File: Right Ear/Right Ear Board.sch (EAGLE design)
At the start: 6 parts, among them J1 502585-0470

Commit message: Update right ear boards
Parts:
- removed C2: (no value), rcl:C-USC0402
- added C4: 10uF, rcl:C-USC0603K
- added SV2, SV3: (no value), con-lstb:MA03-1
- C1: value (none) -> 10uF; device rcl:C-USC0402 -> rcl:C-USC0603K; PARTNO (none) -> GRM188R61A106KE69D
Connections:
- removed net N$1: LED1.DO, LED7.DI
- new net DATA: LED1.DO, LED7.DI, SV2.2, SV3.2
- net +5V: now also C4.1, SV2.1, SV3.3; no longer C2.1
- net GND: now also C4.2, SV2.3, SV3.1; no longer C2.2
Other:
- moved on the sheet: C1
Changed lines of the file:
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@@
 <?xml version="1.0" encoding="utf-8"?>
 <!DOCTYPE eagle SYSTEM "eagle.dtd">
-<eagle version="8.6.0">
+<eagle version="8.5.0">
 <drawing>
 <settings>
@@
 <part name="LED7" library="adafruit" deviceset="WS2812B" device="5050"/>
 <part name="LED1" library="adafruit" deviceset="WS2812B" device="5050"/>
-<part name="C1" library="rcl" library_urn="urn:adsk.eagle:library:334" deviceset="C-US" device="C0402" package3d_urn="urn:adsk.eagle:package:23626/1"/>
 <part name="GND20" library="supply1" deviceset="GND" device=""/>
-<part name="C2" library="rcl" library_urn="urn:adsk.eagle:library:334" deviceset="C-US" device="C0402" package3d_urn="urn:adsk.eagle:package:23626/1"/>
 <part name="GND1" library="supply1" deviceset="GND" device=""/>
 <part name="J1" library="FormE" deviceset="MOLEX_CLICKMATE-4-R/A" device="" value="502585-0470"/>
@@
 <part name="P+2" library="supply1" library_urn="urn:adsk.eagle:library:371" deviceset="+5V" device=""/>
 <part name="P+3" library="supply1" library_urn="urn:adsk.eagle:library:371" deviceset="+5V" device=""/>
+<part name="SV2" library="con-lstb" library_urn="urn:adsk.eagle:library:162" deviceset="MA03-1" device="" package3d_urn="urn:adsk.eagle:package:8339/1"/>
+<part name="SV3" library="con-lstb" library_urn="urn:adsk.eagle:library:162" deviceset="MA03-1" device="" package3d_urn="urn:adsk.eagle:package:8339/1"/>
+<part name="C4" library="rcl" deviceset="C-US" device="C0603K" value="10uF">
+<attribute name="PARTNO" value="GRM188R61A106KE69D"/>
+</part>
+<part name="C1" library="rcl" deviceset="C-US" device="C0603K" value="10uF">
+<attribute name="PARTNO" value="GRM188R61A106KE69D"/>
+</part>
+<part name="P+4" library="supply1" library_urn="urn:adsk.eagle:library:371" deviceset="+5V" device=""/>
 </parts>
 <sheets>
@@
 <instances>
 <instance part="SV1" gate="G$1" x="78.74" y="46.99" rot="MR180"/>
-<instance part="LED7" gate="G$1" x="58.42" y="82.55" rot="MR0"/>
+<instance part="LED7" gate="G$1" x="35.56" y="87.63" rot="MR0"/>
 <instance part="LED1" gate="G$1" x="106.68" y="82.55" rot="MR0"/>
-<instance part="C1" gate="G$1" x="81.28" y="97.79"/>
-<instance part="GND20" gate="1" x="81.28" y="90.17"/>
-<instance part="C2" gate="G$1" x="128.27" y="95.25"/>
-<instance part="GND1" gate="1" x="128.27" y="87.63"/>
+<instance part="GND20" gate="1" x="63.5" y="92.71"/>
+<instance part="GND1" gate="1" x="128.27" y="85.09"/>
 <instance part="J1" gate="G$1" x="165.1" y="49.53"/>
-<instance part="GND2" gate="1" x="58.42" y="61.976"/>
+<instance part="GND2" gate="1" x="35.56" y="67.056"/>
 <instance part="GND3" gate="1" x="106.68" y="61.214"/>
 <instance part="GND4" gate="1" x="91.186" y="34.29"/>
 <instance part="GND5" gate="1" x="151.13" y="41.91"/>
 <instance part="P+1" gate="1" x="152.4" y="60.96"/>
-<instance part="P+2" gate="1" x="53.34" y="106.68"/>
+<instance part="P+2" gate="1" x="30.48" y="111.76"/>
 <instance part="P+3" gate="1" x="86.36" y="58.42"/>
+<instance part="SV2" gate="G$1" x="73.66" y="80.01" rot="MR180"/>
+<instance part="SV3" gate="G$1" x="71.12" y="80.01" rot="MR0"/>
+<instance part="C4" gate="G$1" x="63.5" y="101.6">
+<attribute name="PARTNO" x="63.5" y="101.6" size="1.778" layer="96" display="off"/>
+</instance>
+<instance part="C1" gate="G$1" x="128.27" y="94.488">
+<attribute name="PARTNO" x="128.27" y="94.488" size="1.778" layer="96" display="off"/>
+</instance>
+<instance part="P+4" gate="1" x="127" y="106.68"/>
 </instances>
 <busses>
@@
 </segment>
 <segment>
-<pinref part="C1" gate="G$1" pin="1"/>
-<pinref part="LED7" gate="G$1" pin="VDD"/>
-<wire x1="53.34" y1="97.79" x2="53.34" y2="100.33" width="0.1524" layer="91"/>
-<wire x1="53.34" y1="100.33" x2="53.34" y2="104.14" width="0.1524" layer="91"/>
-<wire x1="81.28" y1="100.33" x2="53.34" y2="100.33" width="0.1524" layer="91"/>
-<junction x="53.34" y="100.33"/>
-<pinref part="LED1" gate="G$1" pin="VDD"/>
-<wire x1="101.6" y1="97.79" x2="101.6" y2="100.33" width="0.1524" layer="91"/>
-<wire x1="81.28" y1="100.33" x2="101.6" y2="100.33" width="0.1524" layer="91"/>
-<junction x="81.28" y="100.33"/>
-<junction x="101.6" y="100.33"/>
-<pinref part="C2" gate="G$1" pin="1"/>
-<wire x1="101.6" y1="100.33" x2="128.27" y2="100.33" width="0.1524" layer="91"/>
-<wire x1="128.27" y1="100.33" x2="128.27" y2="97.79" width="0.1524" layer="91"/>
-<pinref part="P+2" gate="1" pin="+5V"/>
-</segment>
-<segment>
 <pinref part="J1" gate="G$1" pin="1"/>
 <wire x1="162.56" y1="54.61" x2="152.4" y2="54.61" width="0.1524" layer="91"/>
@@
 <pinref part="P+1" gate="1" pin="+5V"/>
 </segment>
+<segment>
+<wire x1="128.27" y1="100.33" x2="128.27" y2="97.028" width="0.1524" layer="91"/>
+<wire x1="101.6" y1="100.33" x2="127" y2="100.33" width="0.1524" layer="91"/>
+<pinref part="LED1" gate="G$1" pin="VDD"/>
+<wire x1="127" y1="100.33" x2="128.27" y2="100.33" width="0.1524" layer="91"/>
+<wire x1="101.6" y1="97.79" x2="101.6" y2="99.06" width="0.1524" layer="91"/>
+<pinref part="SV2" gate="G$1" pin="1"/>
+<wire x1="101.6" y1="99.06" x2="101.6" y2="100.33" width="0.1524" layer="91"/>
+<wire x1="81.28" y1="82.55" x2="81.28" y2="99.06" width="0.1524" layer="91"/>
+<wire x1="81.28" y1="99.06" x2="101.6" y2="99.06" width="0.1524" layer="91"/>
+<junction x="101.6" y="99.06"/>
+<pinref part="C1" gate="G$1" pin="1"/>
+<pinref part="P+4" gate="1" pin="+5V"/>
+<wire x1="127" y1="104.14" x2="127" y2="100.33" width="0.1524" layer="91"/>
+<junction x="127" y="100.33"/>
+</segment>
+<segment>
+<pinref part="LED7" gate="G$1" pin="VDD"/>
+<pinref part="P+2" gate="1" pin="+5V"/>
+<wire x1="30.48" y1="102.87" x2="30.48" y2="106.68" width="0.1524" layer="91"/>
+<pinref part="C4" gate="G$1" pin="1"/>
+<wire x1="30.48" y1="106.68" x2="30.48" y2="109.22" width="0.1524" layer="91"/>
+<wire x1="63.5" y1="104.14" x2="63.5" y2="106.68" width="0.1524" layer="91"/>
+<wire x1="63.5" y1="106.68" x2="53.34" y2="106.68" width="0.1524" layer="91"/>
+<junction x="30.48" y="106.68"/>
+<pinref part="SV3" gate="G$1" pin="3"/>
+<wire x1="53.34" y1="106.68" x2="30.48" y2="106.68" width="0.1524" layer="91"/>
+<wire x1="63.5" y1="82.55" x2="53.34" y2="82.55" width="0.1524" layer="91"/>
+<wire x1="53.34" y1="82.55" x2="53.34" y2="106.68" width="0.1524" layer="91"/>
+<junction x="53.34" y="106.68"/>
+</segment>
 </net>
 <net name="GND" class="0">
-<segment>
-<pinref part="C1" gate="G$1" pin="2"/>
-<pinref part="GND20" gate="1" pin="GND"/>
-</segment>
-<segment>
-<pinref part="C2" gate="G$1" pin="2"/>
-<pinref part="GND1" gate="1" pin="GND"/>
-</segment>
 <segment>
 <pinref part="J1" gate="G$1" pin="4"/>
@@
 <pinref part="LED7" gate="G$1" pin="GND"/>
 <pinref part="GND2" gate="1" pin="GND"/>
-<wire x1="58.42" y1="72.39" x2="58.42" y2="64.516" width="0.1524" layer="91"/>
+<wire x1="35.56" y1="77.47" x2="35.56" y2="69.596" width="0.1524" layer="91"/>
+<pinref part="SV3" gate="G$1" pin="1"/>
+<wire x1="63.5" y1="77.47" x2="35.56" y2="77.47" width="0.1524" layer="91"/>
+<junction x="35.56" y="77.47"/>
 </segment>
 <segment>
 <pinref part="LED1" gate="G$1" pin="GND"/>
 <pinref part="GND3" gate="1" pin="GND"/>
-<wire x1="106.68" y1="72.39" x2="106.68" y2="63.754" width="0.1524" layer="91"/>
+<wire x1="106.68" y1="72.39" x2="106.68" y2="71.12" width="0.1524" layer="91"/>
+<pinref part="SV2" gate="G$1" pin="3"/>
+<wire x1="106.68" y1="71.12" x2="106.68" y2="63.754" width="0.1524" layer="91"/>
+<wire x1="81.28" y1="77.47" x2="81.28" y2="71.12" width="0.1524" layer="91"/>
+<wire x1="81.28" y1="71.12" x2="106.68" y2="71.12" width="0.1524" layer="91"/>
+<junction x="106.68" y="71.12"/>
 </segment>
 <segment>
@@
 <wire x1="86.36" y1="44.45" x2="91.186" y2="44.45" width="0.1524" layer="91"/>
 <wire x1="91.186" y1="44.45" x2="91.186" y2="36.83" width="0.1524" layer="91"/>
+</segment>
+<segment>
+<pinref part="GND20" gate="1" pin="GND"/>
+<pinref part="C4" gate="G$1" pin="2"/>
+<wire x1="63.5" y1="95.25" x2="63.5" y2="96.52" width="0.1524" layer="91"/>
+</segment>
+<segment>
+<pinref part="C1" gate="G$1" pin="2"/>
+<pinref part="GND1" gate="1" pin="GND"/>
+<wire x1="128.27" y1="89.408" x2="128.27" y2="87.63" width="0.1524" layer="91"/>
 </segment>
 </net>
@@
 </segment>
 </net>
-<net name="N$1" class="0">
-<segment>
+<net name="DATA" class="0">
+<segment>
+<pinref part="LED1" gate="G$1" pin="DO"/>
+<pinref part="SV2" gate="G$1" pin="2"/>
+<wire x1="93.98" y1="80.01" x2="81.28" y2="80.01" width="0.1524" layer="91"/>
+<label x="88.138" y="80.01" size="1.778" layer="95"/>
+</segment>
+<segment>
+<pinref part="SV3" gate="G$1" pin="2"/>
 <pinref part="LED7" gate="G$1" pin="DI"/>
-<pinref part="LED1" gate="G$1" pin="DO"/>
-<wire x1="71.12" y1="80.01" x2="93.98" y2="80.01" width="0.1524" layer="91"/>
-</segment>
-</net>
+<wire x1="63.5" y1="80.01" x2="48.26" y2="80.01" width="0.1524" layer="91"/>
+<wire x1="48.26" y1="80.01" x2="48.26" y2="85.09" width="0.1524" layer="91"/>
+<label x="49.022" y="80.01" size="1.778" layer="95"/>
+</segment>
+</net>

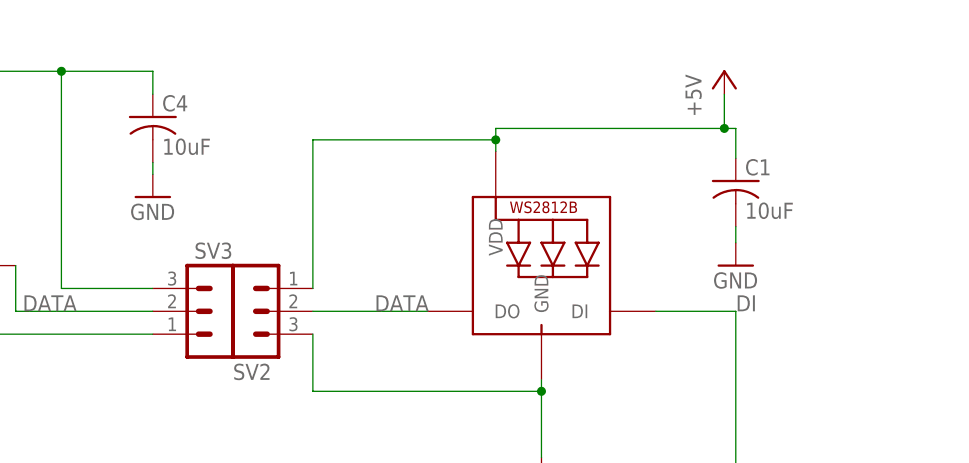
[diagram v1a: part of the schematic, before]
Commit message: Made changes
Change LED caps to .1uF on right ear and center
Add resistor to D2
Add level shifters (1 for D1, 1 for D2)
Add mount holes on right ear
Add mosfet for servo (see things to consider.txt)
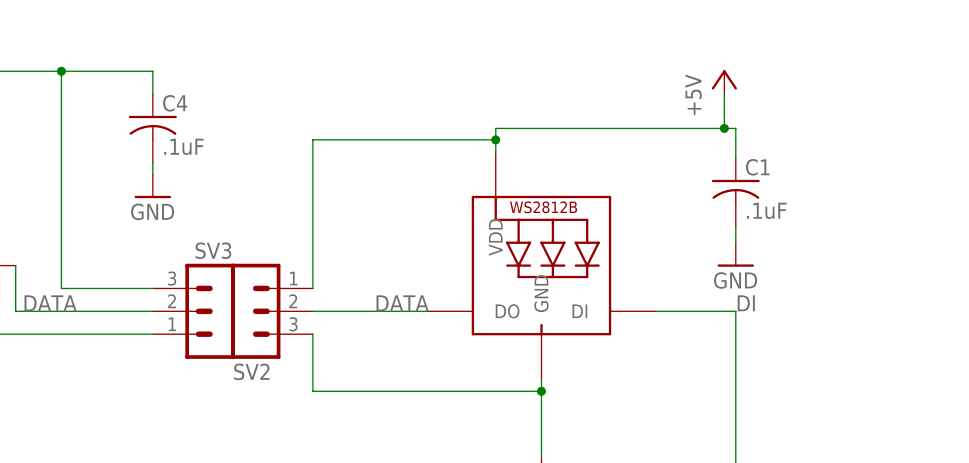
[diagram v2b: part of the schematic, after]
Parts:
- C1, C4: value 10uF -> .1uF
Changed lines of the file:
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@@
 <?xml version="1.0" encoding="utf-8"?>
 <!DOCTYPE eagle SYSTEM "eagle.dtd">
-<eagle version="8.5.0">
+<eagle version="8.3.1">
 <drawing>
 <settings>
@@
 <part name="SV2" library="con-lstb" library_urn="urn:adsk.eagle:library:162" deviceset="MA03-1" device="" package3d_urn="urn:adsk.eagle:package:8339/1"/>
 <part name="SV3" library="con-lstb" library_urn="urn:adsk.eagle:library:162" deviceset="MA03-1" device="" package3d_urn="urn:adsk.eagle:package:8339/1"/>
-<part name="C4" library="rcl" deviceset="C-US" device="C0603K" value="10uF">
+<part name="C4" library="rcl" deviceset="C-US" device="C0603K" value=".1uF">
 <attribute name="PARTNO" value="GRM188R61A106KE69D"/>
 </part>
-<part name="C1" library="rcl" deviceset="C-US" device="C0603K" value="10uF">
+<part name="C1" library="rcl" deviceset="C-US" device="C0603K" value=".1uF">
 <attribute name="PARTNO" value="GRM188R61A106KE69D"/>
 </part>

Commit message: Done with board layouts
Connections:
- net +5V: now also SV1.2; no longer SV1.1
- net SERVO_PWM: now also SV1.1; no longer SV1.2
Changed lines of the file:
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@@
 <?xml version="1.0" encoding="utf-8"?>
 <!DOCTYPE eagle SYSTEM "eagle.dtd">
-<eagle version="8.3.1">
+<eagle version="8.6.1">
 <drawing>
 <settings>
@@
 <net name="+5V" class="0">
 <segment>
-<pinref part="SV1" gate="G$1" pin="1"/>
-<wire x1="86.36" y1="49.53" x2="86.36" y2="55.88" width="0.1524" layer="91"/>
-<label x="87.63" y="55.88" size="1.778" layer="95"/>
-<pinref part="P+3" gate="1" pin="+5V"/>
-</segment>
-<segment>
 <pinref part="J1" gate="G$1" pin="1"/>
 <wire x1="162.56" y1="54.61" x2="152.4" y2="54.61" width="0.1524" layer="91"/>
@@
 <junction x="53.34" y="106.68"/>
 </segment>
+<segment>
+<pinref part="P+3" gate="1" pin="+5V"/>
+<pinref part="SV1" gate="G$1" pin="2"/>
+<wire x1="86.36" y1="55.88" x2="86.36" y2="46.99" width="0.1524" layer="91"/>
+</segment>
 </net>
 <net name="GND" class="0">
@@
 <net name="SERVO_PWM" class="0">
 <segment>
-<pinref part="SV1" gate="G$1" pin="2"/>
-<wire x1="86.36" y1="46.99" x2="91.44" y2="46.99" width="0.1524" layer="91"/>
 <label x="91.44" y="46.99" size="1.778" layer="95"/>
 <pinref part="J1" gate="G$1" pin="3"/>
-<wire x1="162.56" y1="49.53" x2="91.44" y2="49.53" width="0.1524" layer="91"/>
-<wire x1="91.44" y1="49.53" x2="91.44" y2="46.99" width="0.1524" layer="91"/>
+<wire x1="162.56" y1="49.53" x2="86.36" y2="49.53" width="0.1524" layer="91"/>
+<pinref part="SV1" gate="G$1" pin="1"/>
 </segment>
 </net>
